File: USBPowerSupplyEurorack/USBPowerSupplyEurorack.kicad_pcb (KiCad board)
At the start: 2 copper layers, 4 parts, among them J1 1734366-1, T1 RS6-0512D

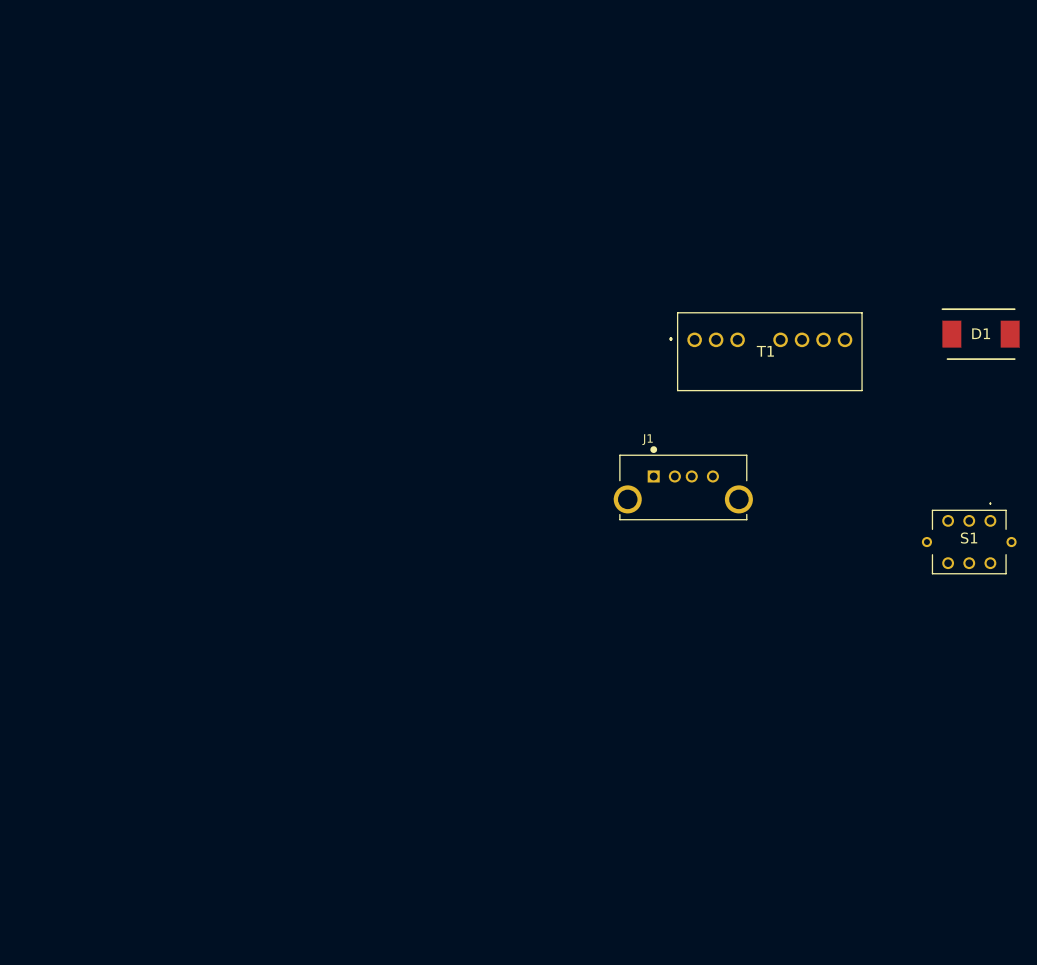
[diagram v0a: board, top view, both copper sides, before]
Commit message: changed diode for lower forward voltage, prepared 2HP PCB contour
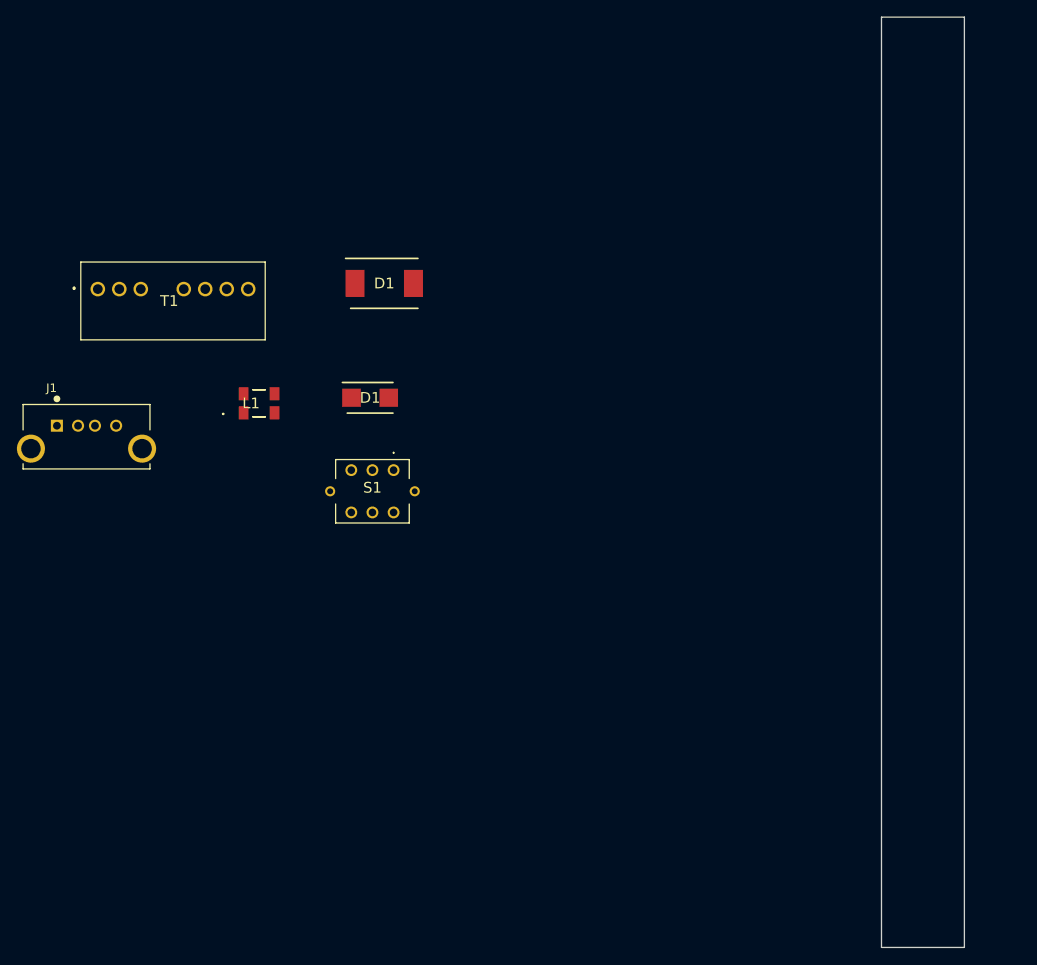
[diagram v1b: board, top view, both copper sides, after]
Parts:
- added D1: LSM115JE3_TR13, LSM115JE3_TR13:DIOM5436X330N, F.Cu at (74.1, 93.1)
- added L1: 744235601, 744235601:744235601, F.Cu at (61.0, 93.8)
- moved S1 70.8 mm to (76.9, 101.7)
- moved J1 70.8 mm to (37.1, 96.4)
- moved T1 70.8 mm to (41.9, 80.3)
- moved D1 70.8 mm to (75.8, 79.6)
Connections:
- J1 pad 1: Net-(J1-Pad1) -> Net-(D1-Pad2)
- J1 pad 4: Net-(J1-Pad4) -> GND
- S1 pad 1: Net-(S1-Pad1) -> +5VD
- S1 pad 2: Net-(S1-Pad2) -> +5VD
- S1 pad 4: Net-(S1-Pad4) -> +5V
- S1 pad 5: Net-(S1-Pad5) -> +5V
- S1 pad L1: Net-(S1-PadL1) -> +5V
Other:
- board outline added: 9.8 x 110 mm

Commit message: completed schematics
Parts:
- moved J1 115.1 mm to (138.3, 151.1), turned to 90 degrees
- moved T1 96.5 mm to (138.1, 72.3), turned to 90 degrees
- moved L1 85.4 mm to (140.5, 124.8)
- moved D1 71.7 mm to (138.6, 114.0), turned to 90 degrees
- moved D1 66.6 mm to (139.6, 105.3)
- moved S1 62.6 mm to (136.9, 83.8), turned to 90 degrees
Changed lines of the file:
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@@
   )
   (module LP4OA1PBCTR:LP4OA1PBCTR (layer F.Cu)
-    (at 76.875 101.675)
+    (at 136.925 83.825 90)
     (descr LP4OA1PBCTR-1)
     (tags Switch)
-    (fp_text reference S1 (at -2.5 2.075) (layer F.SilkS)
-      (effects (font (size 1.27 1.27) (thickness 0.254)))
-    )
-    (fp_text value LP4OA1PBCTR (at -2.5 2.075) (layer F.SilkS) hide
+    (fp_text reference S1 (at -2.5 2.075 90) (layer F.SilkS)
+      (effects (font (size 1.27 1.27) (thickness 0.254)))
+    )
+    (fp_text value LP4OA1PBCTR (at -2.5 2.075 90) (layer F.SilkS) hide
       (effects (font (size 1.27 1.27) (thickness 0.254)))
     )
@@
     (fp_line (start 1.85 -1.25) (end 1.85 6.25) (layer Dwgs.User) (width 0.2))
     (fp_line (start -6.85 -1.25) (end 1.85 -1.25) (layer Dwgs.User) (width 0.2))
-    (pad L2 thru_hole circle (at -7.5 2.5 90) (size 1.2 1.2) (drill 0.7) (layers *.Cu *.Mask F.SilkS)
+    (pad L2 thru_hole circle (at -7.5 2.5 180) (size 1.2 1.2) (drill 0.7) (layers *.Cu *.Mask F.SilkS)
       (net 20 "Net-(R1-Pad1)"))
-    (pad L1 thru_hole circle (at 2.5 2.5 90) (size 1.2 1.2) (drill 0.7) (layers *.Cu *.Mask F.SilkS)
-      (net 17 +5V))
-    (pad 6 thru_hole circle (at -5 5 90) (size 1.4 1.4) (drill 0.9) (layers *.Cu *.Mask F.SilkS)
+    (pad L1 thru_hole circle (at 2.5 2.5 180) (size 1.2 1.2) (drill 0.7) (layers *.Cu *.Mask F.SilkS)
+      (net 17 +5V))
+    (pad 6 thru_hole circle (at -5 5 180) (size 1.4 1.4) (drill 0.9) (layers *.Cu *.Mask F.SilkS)
       (net 13 "Net-(S1-Pad6)"))
-    (pad 5 thru_hole circle (at -2.5 5 90) (size 1.4 1.4) (drill 0.9) (layers *.Cu *.Mask F.SilkS)
-      (net 17 +5V))
-    (pad 4 thru_hole circle (at 0 5 90) (size 1.4 1.4) (drill 0.9) (layers *.Cu *.Mask F.SilkS)
-      (net 17 +5V))
-    (pad 3 thru_hole circle (at -5 0 90) (size 1.4 1.4) (drill 0.9) (layers *.Cu *.Mask F.SilkS)
+    (pad 5 thru_hole circle (at -2.5 5 180) (size 1.4 1.4) (drill 0.9) (layers *.Cu *.Mask F.SilkS)
+      (net 17 +5V))
+    (pad 4 thru_hole circle (at 0 5 180) (size 1.4 1.4) (drill 0.9) (layers *.Cu *.Mask F.SilkS)
+      (net 17 +5V))
+    (pad 3 thru_hole circle (at -5 0 180) (size 1.4 1.4) (drill 0.9) (layers *.Cu *.Mask F.SilkS)
       (net 14 "Net-(S1-Pad3)"))
-    (pad 2 thru_hole circle (at -2.5 0 90) (size 1.4 1.4) (drill 0.9) (layers *.Cu *.Mask F.SilkS)
+    (pad 2 thru_hole circle (at -2.5 0 180) (size 1.4 1.4) (drill 0.9) (layers *.Cu *.Mask F.SilkS)
       (net 15 +5VD))
-    (pad 1 thru_hole circle (at 0 0 90) (size 1.4 1.4) (drill 0.9) (layers *.Cu *.Mask F.SilkS)
+    (pad 1 thru_hole circle (at 0 0 180) (size 1.4 1.4) (drill 0.9) (layers *.Cu *.Mask F.SilkS)
       (net 15 +5VD))
   )
   (module 744235601:744235601 (layer F.Cu)
-    (at 60.975 93.78)
+    (at 140.5 124.8)
     (descr 744235601-3)
     (tags Inductor)
@@
   )
   (module LSM115JE3_TR13:DIOM5436X330N (layer F.Cu)
-    (at 74.1 93.125)
+    (at 139.575 105.35)
     (descr do-214ba)
     (tags "Schottky Diode")
@@
   )
   (module RS6-0512D:RS60505S (layer F.Cu)
-    (at 41.91 80.275)
+    (at 138.1 72.325 90)
     (descr RS6)
     (tags Transformer)
-    (fp_text reference T1 (at 8.445 1.4) (layer F.SilkS)
-      (effects (font (size 1.27 1.27) (thickness 0.254)))
-    )
-    (fp_text value RS6-0512D (at 8.445 1.4) (layer F.SilkS) hide
+    (fp_text reference T1 (at 8.445 1.4 90) (layer F.SilkS)
+      (effects (font (size 1.27 1.27) (thickness 0.254)))
+    )
+    (fp_text value RS6-0512D (at 8.445 1.4 90) (layer F.SilkS) hide
       (effects (font (size 1.27 1.27) (thickness 0.254)))
     )
@@
     (fp_arc (start -2.8 -0.1) (end -2.8 0) (angle -180) (layer F.SilkS) (width 0.2))
     (fp_arc (start -2.8 -0.1) (end -2.8 -0.2) (angle -180) (layer F.SilkS) (width 0.2))
-    (pad 8 thru_hole circle (at 17.78 0 90) (size 1.725 1.725) (drill 1.15) (layers *.Cu *.Mask F.SilkS)
+    (pad 8 thru_hole circle (at 17.78 0 180) (size 1.725 1.725) (drill 1.15) (layers *.Cu *.Mask F.SilkS)
       (net 6 -Vout))
-    (pad 7 thru_hole circle (at 15.24 0 90) (size 1.725 1.725) (drill 1.15) (layers *.Cu *.Mask F.SilkS)
+    (pad 7 thru_hole circle (at 15.24 0 180) (size 1.725 1.725) (drill 1.15) (layers *.Cu *.Mask F.SilkS)
       (net 7 "Net-(T1-Pad7)"))
-    (pad 6 thru_hole circle (at 12.7 0 90) (size 1.725 1.725) (drill 1.15) (layers *.Cu *.Mask F.SilkS)
+    (pad 6 thru_hole circle (at 12.7 0 180) (size 1.725 1.725) (drill 1.15) (layers *.Cu *.Mask F.SilkS)
       (net 8 +Vout))
-    (pad 5 thru_hole circle (at 10.16 0 90) (size 1.725 1.725) (drill 1.15) (layers *.Cu *.Mask F.SilkS)
+    (pad 5 thru_hole circle (at 10.16 0 180) (size 1.725 1.725) (drill 1.15) (layers *.Cu *.Mask F.SilkS)
       (net 9 "Net-(T1-Pad5)"))
-    (pad 3 thru_hole circle (at 5.08 0 90) (size 1.725 1.725) (drill 1.15) (layers *.Cu *.Mask F.SilkS)
+    (pad 3 thru_hole circle (at 5.08 0 180) (size 1.725 1.725) (drill 1.15) (layers *.Cu *.Mask F.SilkS)
       (net 10 "Net-(T1-Pad3)"))
-    (pad 2 thru_hole circle (at 2.54 0 90) (size 1.725 1.725) (drill 1.15) (layers *.Cu *.Mask F.SilkS)
+    (pad 2 thru_hole circle (at 2.54 0 180) (size 1.725 1.725) (drill 1.15) (layers *.Cu *.Mask F.SilkS)
       (net 11 +Vin))
-    (pad 1 thru_hole circle (at 0 0 90) (size 1.725 1.725) (drill 1.15) (layers *.Cu *.Mask F.SilkS)
+    (pad 1 thru_hole circle (at 0 0 180) (size 1.725 1.725) (drill 1.15) (layers *.Cu *.Mask F.SilkS)
       (net 12 -Vin))
   )
   (module 1734366-1:TE_1734366-1 (layer F.Cu)
-    (at 37.075 96.425)
-    (fp_text reference J1 (at -0.63622 -4.45354) (layer F.SilkS)
+    (at 138.325 151.075 90)
+    (fp_text reference J1 (at -0.63622 -4.45354 90) (layer F.SilkS)
       (effects (font (size 1.001921 1.001921) (thickness 0.015)))
     )
-    (fp_text value 1734366-1 (at 3.81319 6.99082) (layer F.Fab)
+    (fp_text value 1734366-1 (at 3.81319 6.99082 90) (layer F.Fab)
       (effects (font (size 1.000835 1.000835) (thickness 0.015)))
     )
@@
     (fp_circle (center 0 -3.175) (end 0.2 -3.175) (layer F.SilkS) (width 0.4))
     (fp_circle (center 0 -1.27) (end 0.2 -1.27) (layer F.Fab) (width 0.4))
-    (pad SH2 thru_hole circle (at 10.07 2.71) (size 3.316 3.316) (drill 2.3) (layers *.Cu *.Mask)
+    (pad SH2 thru_hole circle (at 10.07 2.71 90) (size 3.316 3.316) (drill 2.3) (layers *.Cu *.Mask)
       (net 3 "Net-(J1-PadSH1)"))
-    (pad SH1 thru_hole circle (at -3.07 2.71) (size 3.316 3.316) (drill 2.3) (layers *.Cu *.Mask)
+    (pad SH1 thru_hole circle (at -3.07 2.71 90) (size 3.316 3.316) (drill 2.3) (layers *.Cu *.Mask)
       (net 3 "Net-(J1-PadSH1)"))
-    (pad 4 thru_hole circle (at 7 0) (size 1.428 1.428) (drill 0.92) (layers *.Cu *.Mask)
+    (pad 4 thru_hole circle (at 7 0 90) (size 1.428 1.428) (drill 0.92) (layers *.Cu *.Mask)
       (net 16 GND))
-    (pad 3 thru_hole circle (at 4.5 0) (size 1.428 1.428) (drill 0.92) (layers *.Cu *.Mask)
+    (pad 3 thru_hole circle (at 4.5 0 90) (size 1.428 1.428) (drill 0.92) (layers *.Cu *.Mask)
       (net 4 "Net-(J1-Pad3)"))
-    (pad 2 thru_hole circle (at 2.5 0) (size 1.428 1.428) (drill 0.92) (layers *.Cu *.Mask)
+    (pad 2 thru_hole circle (at 2.5 0 90) (size 1.428 1.428) (drill 0.92) (layers *.Cu *.Mask)
       (net 5 "Net-(J1-Pad2)"))
-    (pad 1 thru_hole rect (at 0 0) (size 1.428 1.428) (drill 0.92) (layers *.Cu *.Mask)
+    (pad 1 thru_hole rect (at 0 0 90) (size 1.428 1.428) (drill 0.92) (layers *.Cu *.Mask)
       (net 1 "Net-(D1-Pad2)"))
   )
   (module SS36:DIOM8059X265N (layer F.Cu)
-    (at 75.775 79.6)
+    (at 138.625 114.05 90)
     (descr "SMC CASE 403AG ISSUE O")
     (tags "Schottky Diode")
     (attr smd)
-    (fp_text reference D1 (at 0 0) (layer F.SilkS)
-      (effects (font (size 1.27 1.27) (thickness 0.254)))
-    )
-    (fp_text value SS36 (at 0 0) (layer F.SilkS) hide
+    (fp_text reference D1 (at 0 0 90) (layer F.SilkS)
+      (effects (font (size 1.27 1.27) (thickness 0.254)))
+    )
+    (fp_text value SS36 (at 0 0 90) (layer F.SilkS) hide
       (effects (font (size 1.27 1.27) (thickness 0.254)))
     )
@@
     (fp_line (start 4.825 -3.375) (end 4.825 3.375) (layer Dwgs.User) (width 0.05))
     (fp_line (start -4.825 -3.375) (end 4.825 -3.375) (layer Dwgs.User) (width 0.05))
-    (pad 2 smd rect (at 3.45 0) (size 2.25 3.2) (layers F.Cu F.Paste F.Mask)
+    (pad 2 smd rect (at 3.45 0 90) (size 2.25 3.2) (layers F.Cu F.Paste F.Mask)
       (net 1 "Net-(D1-Pad2)"))
-    (pad 1 smd rect (at -3.45 0) (size 2.25 3.2) (layers F.Cu F.Paste F.Mask)
+    (pad 1 smd rect (at -3.45 0 90) (size 2.25 3.2) (layers F.Cu F.Paste F.Mask)
       (net 2 "Net-(D1-Pad1)"))
   )

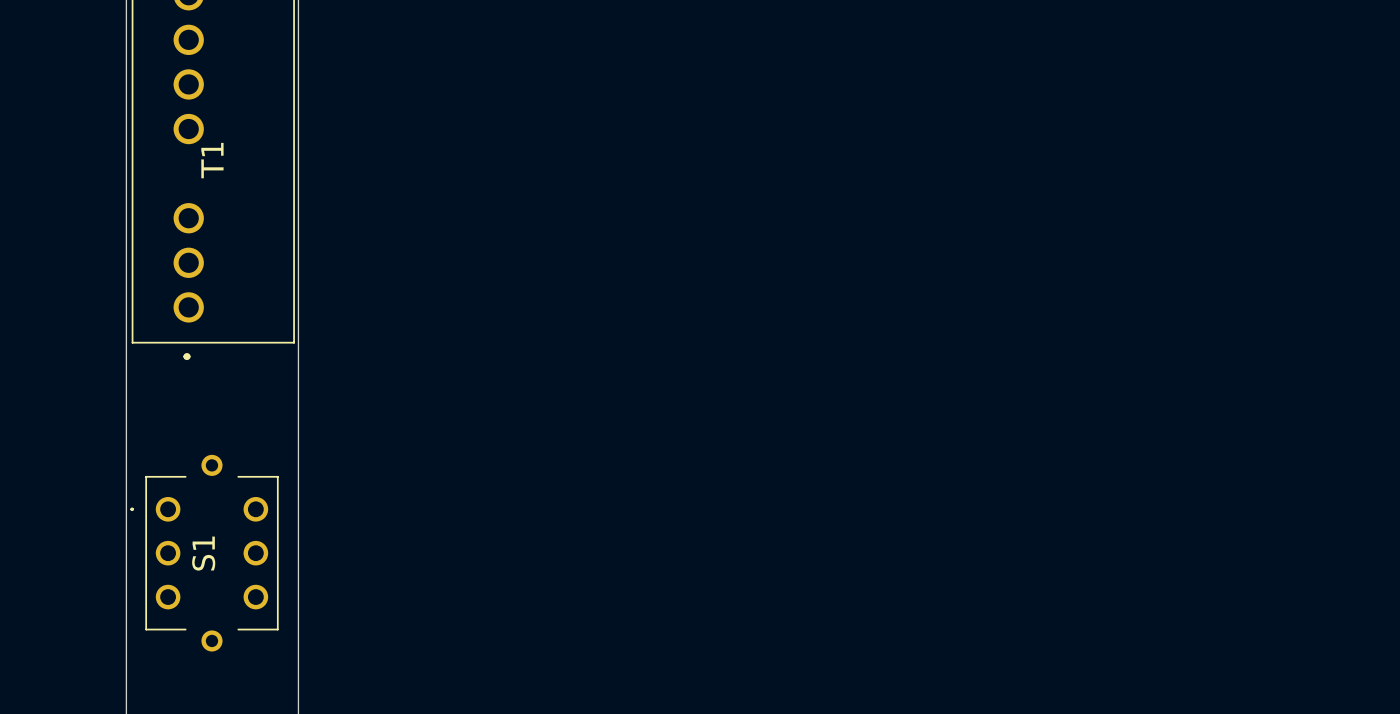
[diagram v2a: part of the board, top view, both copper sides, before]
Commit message: changed TVS symbol as footprint was not valid
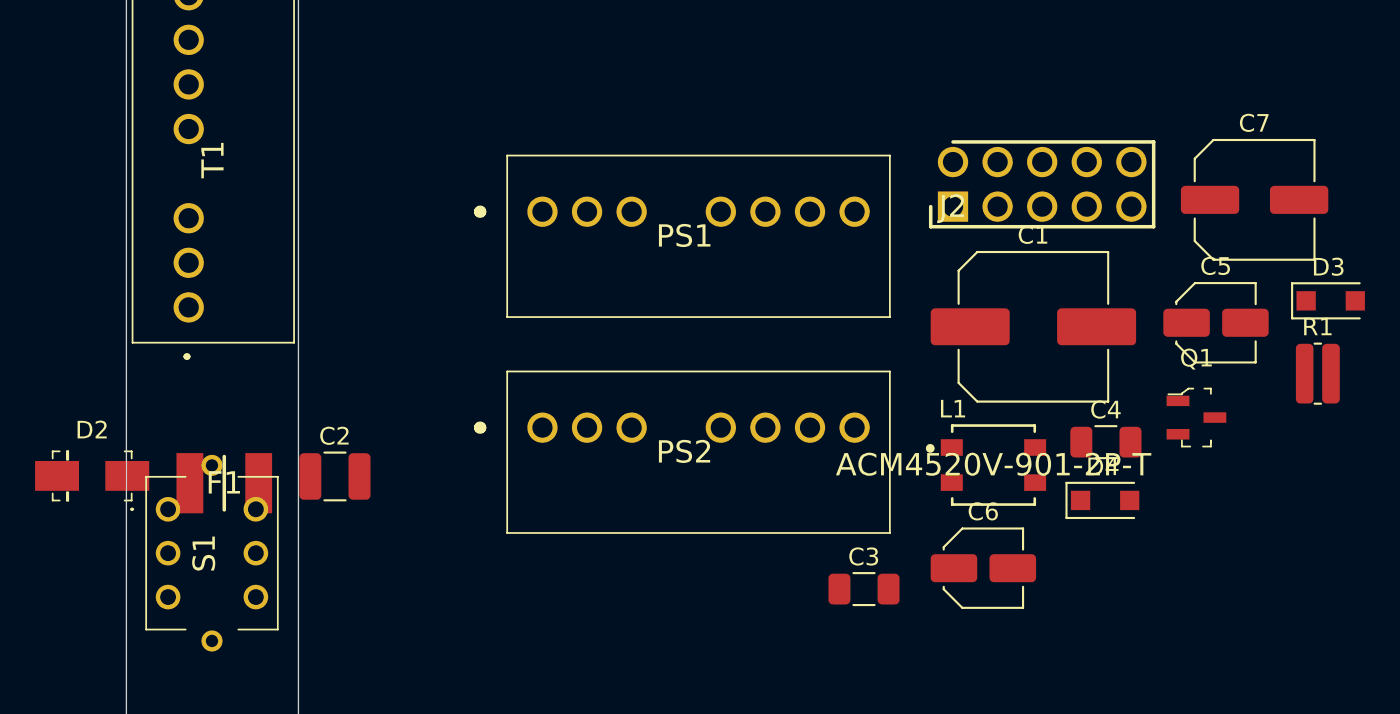
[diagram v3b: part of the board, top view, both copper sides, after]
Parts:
- added C1: 220uF, Capacitor_SMD:C_Elec_8x10.2, F.Cu at (186.2, 73.4)
- added C2: 22uFMLCC, Capacitor_SMD:C_1210_3225Metric, F.Cu at (146.4, 82.0)
- added C3: 100nF MLCC, Capacitor_SMD:C_1206_3216Metric, F.Cu at (176.6, 88.4)
- added C4: 100nF MLCC, Capacitor_SMD:C_1206_3216Metric, F.Cu at (190.3, 80.0)
- added C5: 1uF, Capacitor_SMD:C_Elec_4x5.4, F.Cu at (196.6, 73.2)
- added C6: 1uF, Capacitor_SMD:C_Elec_4x5.4, F.Cu at (183.4, 87.2)
- added C7: 47uF, Capacitor_SMD:C_Elec_6.3x5.8, F.Cu at (198.8, 66.2)
- added D2: SMAJ5.0CA, digikey-footprints:DO-214AC, F.Cu at (132.6, 81.9)
- added D3: 1N4004, Diode_SMD:D_SOD-123F, F.Cu at (203.2, 72.0)
- added D4: 1N4004, Diode_SMD:D_SOD-123F, F.Cu at (190.3, 83.3)
- added F1: 1812L110, 1812L110_16DR:FUSC4632X125N, F.Cu at (140.1, 82.3)
- added J2: 10129381-910001BLF, 10129381-910001BLF:HDRV10W67P254_2X5_1270X483X858P, F.Cu at (181.6, 66.6)
- added L1: ACM4520V-901-2P-T, eec2:TDK-ACM4520V-901-2P-T-0, F.Cu at (183.9, 81.3)
- added PS1: RS6-0512S, RS6-0512S:RS60512S, F.Cu at (158.3, 66.9)
- added PS2: RS6-0512S, RS6-0512S:RS60512S, F.Cu at (158.3, 79.2)
- added Q1: Q_PMOS_GSD, digikey-footprints:SOT-23-3, F.Cu at (195.5, 78.6)
- added R1: 510, Resistor_SMD:R_0612_1632Metric, F.Cu at (202.4, 76.1)
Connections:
- J1 pad 1: Net-(D1-Pad2) -> Net-(F1-Pad1)
- J1 pad 4: GND -> +5V
- S1 pad L1: +5V -> +12V
